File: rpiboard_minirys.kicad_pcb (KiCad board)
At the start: 4 copper layers, 65 x 56.5 mm, 92 parts, among them IC1 LM51231QRGRRQ1, IC2 TPS564242DRLR, IC3 L6470HTR, IC4 L6470HTR, J1 RPi_GPIO, J10 ToF1_Sensor, J11 ToF2_Sensor, J12 ToF3_Sensor, J13 ToF4_Sensor, J14 ToF5_Sensor, J15 ToF6_Sensor, J16 SPI_Interface, J17 UART_Interface, J18 Fan_Interface, J2 Motor_L, J3 Motor_R, J4 B_Cell_3, J5 B_Cell_2, J6 B_Cell_1, J7 SW, J8 Temp_Sensor, J9 IMU_Sensor, Q1 ISK057N04LM6ATLA1, Q2 ISK057N04LM6ATLA1

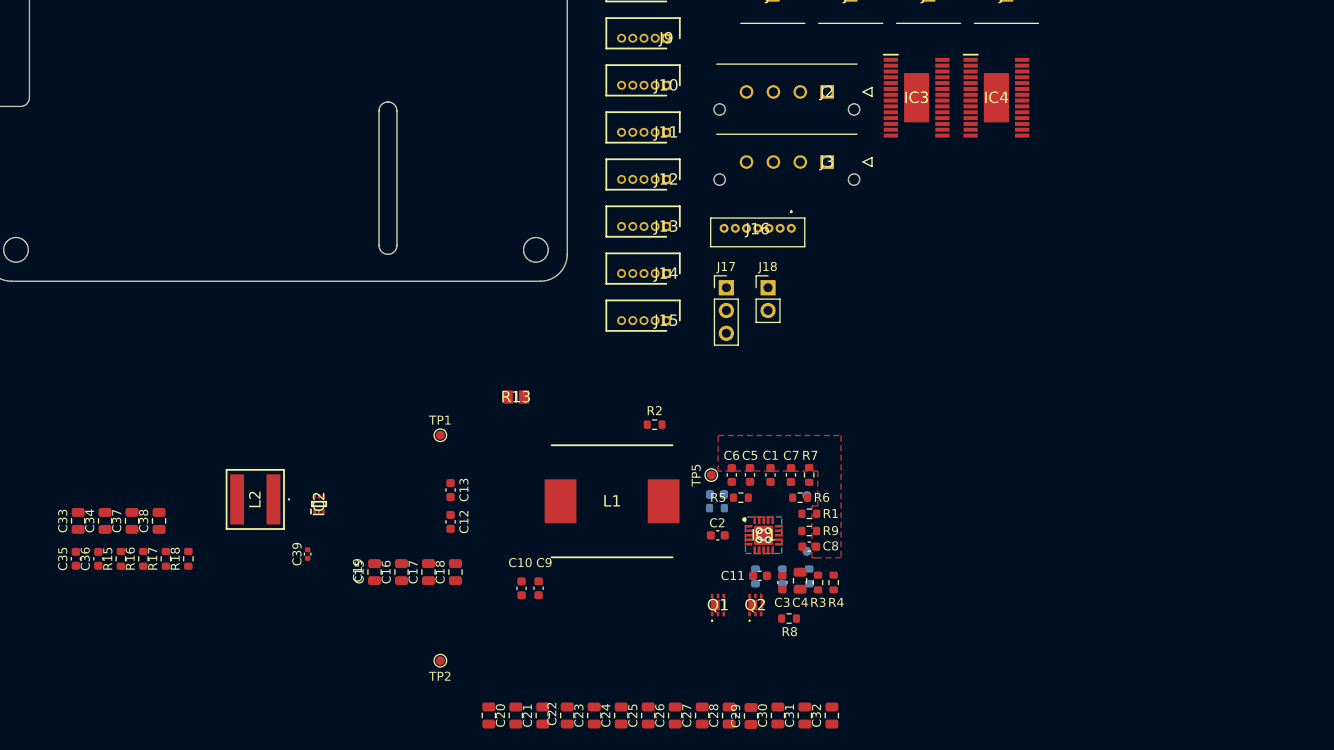
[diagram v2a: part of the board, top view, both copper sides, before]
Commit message: New complete schematic version
May need to resize the resistors, also need to change the caps back to electrolytic
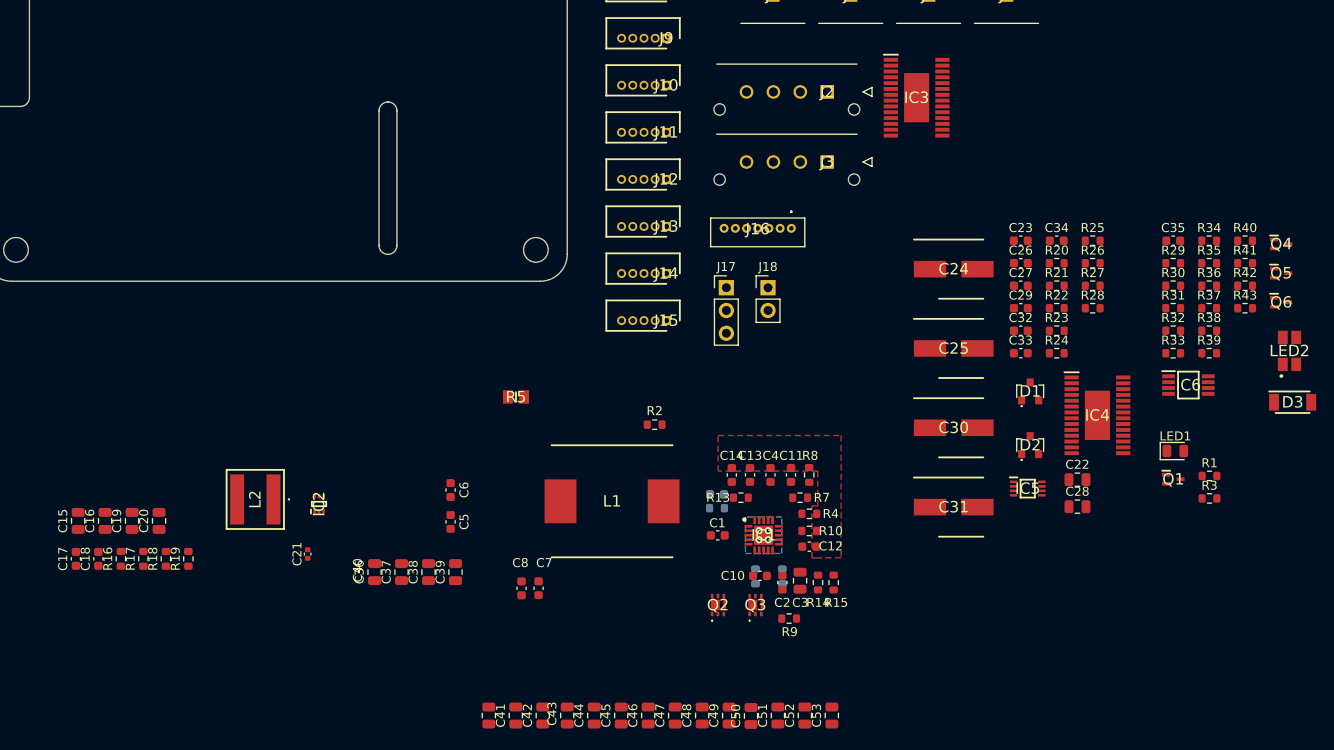
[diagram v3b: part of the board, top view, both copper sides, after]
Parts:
- removed the R12 at (197.5, 143.7)
- removed TP1: TestPoint_VCC, TestPoint:TestPoint_Pad_D1.0mm
- removed TP2: TestPoint_VOUT, TestPoint:TestPoint_Pad_D1.0mm
- removed TP3: TestPoint_TRK, TestPoint:TestPoint_Pad_D1.0mm
- removed TP4: TestPoint_UVLO, TestPoint:TestPoint_Pad_D1.0mm
- removed TP5: TestPoint_SW, TestPoint:TestPoint_Pad_D1.0mm
- added C22: 10uF, Capacitor_SMD:C_0805_2012Metric, F.Cu at (227.4, 132.9)
- added C23: 10nF, Capacitor_SMD:C_0603_1608Metric, F.Cu at (221.1, 106.2)
- added C24: 47uF, parts:CAPAE660X850N, F.Cu at (213.6, 109.4)
- added C25: 47uF, parts:CAPAE660X850N, F.Cu at (213.6, 118.2)
- added C26: 100nF, Capacitor_SMD:C_0603_1608Metric, F.Cu at (221.1, 108.7)
- added C27: 100nF, Capacitor_SMD:C_0603_1608Metric, F.Cu at (221.1, 111.2)
- added C28: 10uF, Capacitor_SMD:C_0805_2012Metric, F.Cu at (227.4, 135.9)
- added C29: 10nF, Capacitor_SMD:C_0603_1608Metric, F.Cu at (221.1, 113.8)
- added C30: 47uF, parts:CAPAE660X850N, F.Cu at (213.6, 127.1)
- added C31: 47uF, parts:CAPAE660X850N, F.Cu at (213.6, 135.9)
- added C32: 100nF, Capacitor_SMD:C_0603_1608Metric, F.Cu at (221.1, 116.3)
- added C33: 100nF, Capacitor_SMD:C_0603_1608Metric, F.Cu at (221.1, 118.8)
- added C34: 100nF, Capacitor_SMD:C_0603_1608Metric, F.Cu at (225.1, 106.2)
- added C35: 100nF, Capacitor_SMD:C_0603_1608Metric, F.Cu at (238.1, 106.2)
- added D1: BAV99, parts:ZXMP6A13FTA, F.Cu at (222.1, 123.0)
- added D2: BAV99, parts:ZXMP6A13FTA, F.Cu at (222.1, 129.0)
- added D3: STPST1H100AF, parts:SODFL4724X103N, F.Cu at (251.4, 124.2)
- added IC5: 74AUP2G00DC,125, parts:SOP50P310X100-8N, F.Cu at (221.9, 133.9)
- added IC6: MAX11613EUA+T, parts:SOP65P490X110-8N, F.Cu at (239.8, 122.3)
- added LED1: GREEN, Diode_SMD:D_0805_2012Metric, F.Cu at (238.3, 129.7)
- added LED2: LSG_T676-P7Q7-1+N7P7-24, parts:LSGT676P7Q71N7P724, F.Cu at (251.1, 118.5)
- added Q1: DMG1012T-7, parts:SOT50P160X80-3N, F.Cu at (238.1, 132.8)
- added Q4: DMG1012T-7, parts:SOT50P160X80-3N, F.Cu at (250.2, 106.6)
- added Q5: DMG1012T-7, parts:SOT50P160X80-3N, F.Cu at (250.2, 109.8)
- added Q6: DMG1012T-7, parts:SOT50P160X80-3N, F.Cu at (250.2, 113.1)
- added R1: 100R, Resistor_SMD:R_0603_1608Metric, F.Cu at (242.2, 132.5)
- added R20: 10k, Resistor_SMD:R_0603_1608Metric, F.Cu at (225.1, 108.7)
- added R21: 27k, Resistor_SMD:R_0603_1608Metric, F.Cu at (225.1, 111.2)
- added R22: 10k, Resistor_SMD:R_0603_1608Metric, F.Cu at (225.1, 113.8)
- added R23: 27k, Resistor_SMD:R_0603_1608Metric, F.Cu at (225.1, 116.3)
- added R24: 38.3k, Resistor_SMD:R_0603_1608Metric, F.Cu at (225.1, 118.8)
- added R25: 38.3k, Resistor_SMD:R_0603_1608Metric, F.Cu at (229.1, 106.2)
- added R26: 38.3k, Resistor_SMD:R_0603_1608Metric, F.Cu at (229.1, 108.7)
- added R27: 38.3k, Resistor_SMD:R_0603_1608Metric, F.Cu at (229.1, 111.2)
- added R28: 38.3k, Resistor_SMD:R_0603_1608Metric, F.Cu at (229.1, 113.8)
- added R29: 100k, Resistor_SMD:R_0603_1608Metric, F.Cu at (238.1, 108.7)
- added R3: 150R, Resistor_SMD:R_0603_1608Metric, F.Cu at (242.2, 135.0)
- added R30: 150R, Resistor_SMD:R_0603_1608Metric, F.Cu at (238.1, 111.2)
- added R31: 15k, Resistor_SMD:R_0603_1608Metric, F.Cu at (238.1, 113.8)
- added R32: 10k, Resistor_SMD:R_0603_1608Metric, F.Cu at (238.1, 116.3)
- added R33: 36k, Resistor_SMD:R_0603_1608Metric, F.Cu at (238.1, 118.8)
- added R34: 10k, Resistor_SMD:R_0603_1608Metric, F.Cu at (242.1, 106.2)
- added R35: 56k, Resistor_SMD:R_0603_1608Metric, F.Cu at (242.1, 108.7)
- added R36: 10k, Resistor_SMD:R_0603_1608Metric, F.Cu at (242.1, 111.2)
- added R37: 10k, Resistor_SMD:R_0603_1608Metric, F.Cu at (242.1, 113.8)
- added R38: 100k, Resistor_SMD:R_0603_1608Metric, F.Cu at (242.1, 116.3)
- added R39: 150R, Resistor_SMD:R_0603_1608Metric, F.Cu at (242.1, 118.8)
- added R40: 150R, Resistor_SMD:R_0603_1608Metric, F.Cu at (246.1, 106.2)
- added R41: 150R, Resistor_SMD:R_0603_1608Metric, F.Cu at (246.1, 108.7)
- added R42: 150R, Resistor_SMD:R_0603_1608Metric, F.Cu at (246.1, 111.2)
- added R43: 100k, Resistor_SMD:R_0603_1608Metric, F.Cu at (246.1, 113.8)
- J16: value SPI_Interface -> SPI_Connector
- J17: value UART_Interface -> UART_Connector
- J18: value Fan_Interface -> Fan_Connector
- R2: value 100k -> 12k
- moved IC4 37.2 mm to (229.6, 125.7)
- renumbered C2 to C1, C11 to C10, C7 to C11, C8 to C12, C5 to C13, C6 to C14, C33 to C15, C34 to C16, C35 to C17, C36 to C18, C37 to C19, C3 to C2, C38 to C20, C39 to C21, C4 to C3, C15 to C36, C16 to C37, C17 to C38, C18 to C39, C1 to C4, C19 to C40, C20 to C41, C21 to C42, C22 to C43, C23 to C44, C24 to C45, C25 to C46, C26 to C47, C27 to C48, C28 to C49, C12 to C5, C29 to C50, C30 to C51, C31 to C52, C32 to C53, C13 to C6, C9 to C7, C10 to C8, C14 to C9, Q1 to Q2, Q2 to Q3, R9 to R10, R10 to R11, R11 to R12, R5 to R13, R3 to R14, R4 to R15, R15 to R16, R16 to R17, R17 to R18, R18 to R19, R1 to R4, R13 to R5, R14 to R6, R6 to R7, R7 to R8, R8 to R9
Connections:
- net /Supply_24V/PGOOD renamed Net-(IC1-PGOOD)
- C1 pad 2: /Supply_24V/VOUT -> +24V
- C18 pad 1: /Supply_5V/+5V -> +5V
- C19 pad 1: /Supply_5V/+5V -> +5V
- C20 pad 1: /Supply_5V/+5V -> +5V
- C21 pad 2: /Supply_5V/+5V -> +5V
- C41 pad 1: /Supply_24V/VOUT -> +24V
- C42 pad 1: /Supply_24V/VOUT -> +24V
- C43 pad 1: /Supply_24V/VOUT -> +24V
- C44 pad 1: /Supply_24V/VOUT -> +24V
- C45 pad 1: /Supply_24V/VOUT -> +24V
- C46 pad 1: /Supply_24V/VOUT -> +24V
- C47 pad 1: /Supply_24V/VOUT -> +24V
- C48 pad 1: /Supply_24V/VOUT -> +24V
- C49 pad 1: /Supply_24V/VOUT -> +24V
- C50 pad 1: /Supply_24V/VOUT -> +24V
- C51 pad 1: /Supply_24V/VOUT -> +24V
- C52 pad 1: /Supply_24V/VOUT -> +24V
- C53 pad 1: /Supply_24V/VOUT -> +24V
- C7 pad 1: /Supply_24V/VOUT -> +24V
- C8 pad 1: /Supply_24V/VOUT -> +24V
- IC1 pad 3: /Supply_24V/VOUT -> +24V
- IC3 pad 1: unconnected-(IC3-OUT1A-Pad1) -> /Connectors/ML_OUT1A
- IC3 pad 10: unconnected-(IC3-CP-Pad10) -> /Motor_Controllers/ML_CP
- IC3 pad 11: unconnected-(IC3-VBOOT-Pad11) -> /Motor_Controllers/ML_VBOOT
- IC3 pad 12: unconnected-(IC3-VSB_1-Pad12) -> +24V
- IC3 pad 13: unconnected-(IC3-PGND_1-Pad13) -> GND
- IC3 pad 14: unconnected-(IC3-OUT1B-Pad14) -> /Connectors/ML_OUT1B
- IC3 pad 15: unconnected-(IC3-OUT2B-Pad15) -> /Connectors/ML_OUT2B
- IC3 pad 16: unconnected-(IC3-VSB_2-Pad16) -> +24V
- IC3 pad 17: unconnected-(IC3-VDD-Pad17) -> +3.3V
- IC3 pad 18: unconnected-(IC3-SDO-Pad18) -> /Motor_Controllers/SPI_BRIDGE
- IC3 pad 19: unconnected-(IC3-CK-Pad19) -> /Connectors/SPI_CLK
- IC3 pad 2: unconnected-(IC3-VSA_1-Pad2) -> +24V
- IC3 pad 20: unconnected-(IC3-SDI-Pad20) -> /Connectors/SPI_MOSI
- IC3 pad 21: unconnected-(IC3-DGND-Pad21) -> GND
- IC3 pad 22: unconnected-(IC3-~{BUSY}/SYNC-Pad22) -> /Motor_Controllers/~{ML_BUSY}
- IC3 pad 23: unconnected-(IC3-~{CS}-Pad23) -> /Connectors/~{SPI_CS_M}
- IC3 pad 24: unconnected-(IC3-~{FLAG}-Pad24) -> /Motor_Controllers/~{ML_FLAG}
- IC3 pad 26: unconnected-(IC3-VSA_2-Pad26) -> +24V
- IC3 pad 27: unconnected-(IC3-PGND_2-Pad27) -> GND
- IC3 pad 28: unconnected-(IC3-OUT2A-Pad28) -> /Connectors/ML_OUT2A
- IC3 pad 29: unconnected-(IC3-EP-Pad29) -> GND
- IC3 pad 3: unconnected-(IC3-~{STBY}/RST-Pad3) -> /Connectors/~{M_STBY}
- IC3 pad 4: unconnected-(IC3-SW-Pad4) -> +3.3V
- IC3 pad 5: unconnected-(IC3-ADCIN-Pad5) -> /Motor_Controllers/ML_ADCIN
- IC3 pad 6: unconnected-(IC3-VREG-Pad6) -> +3.3V
- IC3 pad 8: unconnected-(IC3-OSCOUT-Pad8) -> /Motor_Controllers/OSCOUT
- IC3 pad 9: unconnected-(IC3-AGND-Pad9) -> GND
- IC4 pad 1: unconnected-(IC4-OUT1A-Pad1) -> /Connectors/MR_OUT1A
- IC4 pad 10: unconnected-(IC4-CP-Pad10) -> /Motor_Controllers/MR_CP
- IC4 pad 11: unconnected-(IC4-VBOOT-Pad11) -> /Motor_Controllers/MR_VBOOT
- IC4 pad 12: unconnected-(IC4-VSB_1-Pad12) -> +24V
- IC4 pad 13: unconnected-(IC4-PGND_1-Pad13) -> GND
- IC4 pad 14: unconnected-(IC4-OUT1B-Pad14) -> /Connectors/MR_OUT1B
- IC4 pad 15: unconnected-(IC4-OUT2B-Pad15) -> /Connectors/MR_OUT2B
- IC4 pad 16: unconnected-(IC4-VSB_2-Pad16) -> +24V
- IC4 pad 17: unconnected-(IC4-VDD-Pad17) -> +3.3V
- IC4 pad 18: unconnected-(IC4-SDO-Pad18) -> /Connectors/SPI_MISO
- IC4 pad 19: unconnected-(IC4-CK-Pad19) -> /Connectors/SPI_CLK
- IC4 pad 2: unconnected-(IC4-VSA_1-Pad2) -> +24V
- IC4 pad 20: unconnected-(IC4-SDI-Pad20) -> /Motor_Controllers/SPI_BRIDGE
- IC4 pad 21: unconnected-(IC4-DGND-Pad21) -> GND
- IC4 pad 22: unconnected-(IC4-~{BUSY}/SYNC-Pad22) -> /Motor_Controllers/~{MR_BUSY}
- IC4 pad 23: unconnected-(IC4-~{CS}-Pad23) -> /Connectors/~{SPI_CS_M}
- IC4 pad 24: unconnected-(IC4-~{FLAG}-Pad24) -> /Motor_Controllers/~{MR_FLAG}
- IC4 pad 26: unconnected-(IC4-VSA_2-Pad26) -> +24V
- IC4 pad 27: unconnected-(IC4-PGND_2-Pad27) -> GND
- IC4 pad 28: unconnected-(IC4-OUT2A-Pad28) -> /Connectors/MR_OUT2A
- IC4 pad 29: unconnected-(IC4-EP-Pad29) -> GND
- IC4 pad 3: unconnected-(IC4-~{STBY}/RST-Pad3) -> /Connectors/~{M_STBY}
- IC4 pad 4: unconnected-(IC4-SW-Pad4) -> +3.3V
- IC4 pad 5: unconnected-(IC4-ADCIN-Pad5) -> /Motor_Controllers/MR_ADCIN
- IC4 pad 6: unconnected-(IC4-VREG-Pad6) -> +3.3V
- IC4 pad 8: unconnected-(IC4-OSCOUT-Pad8) -> /Motor_Controllers/OSCOUT
- IC4 pad 9: unconnected-(IC4-AGND-Pad9) -> GND
- J1 pad 1: unconnected-(J1-Pin_1-Pad1) -> +3.3V
- J1 pad 10: unconnected-(J1-Pin_10-Pad10) -> /Connectors/UART_RX
- J1 pad 11: unconnected-(J1-Pin_11-Pad11) -> /Connectors/M_FLAG
- J1 pad 12: unconnected-(J1-Pin_12-Pad12) -> /Connectors/FAN_PWM
- J1 pad 13: unconnected-(J1-Pin_13-Pad13) -> /Connectors/M_BUSY
- J1 pad 14: unconnected-(J1-Pin_14-Pad14) -> GND
- J1 pad 15: unconnected-(J1-Pin_15-Pad15) -> /Connectors/~{M_STBY}
- J1 pad 16: unconnected-(J1-Pin_16-Pad16) -> /Connectors/LED_RED
- J1 pad 17: unconnected-(J1-Pin_17-Pad17) -> +3.3V
- J1 pad 18: unconnected-(J1-Pin_18-Pad18) -> /Connectors/LED_GREEN
- J1 pad 19: unconnected-(J1-Pin_19-Pad19) -> /Connectors/SPI_MOSI
- J1 pad 2: unconnected-(J1-Pin_2-Pad2) -> +5V
- J1 pad 20: unconnected-(J1-Pin_20-Pad20) -> GND
- J1 pad 21: unconnected-(J1-Pin_21-Pad21) -> /Connectors/SPI_MISO
- J1 pad 22: unconnected-(J1-Pin_22-Pad22) -> /Connectors/SPI_IRQ
- J1 pad 23: unconnected-(J1-Pin_23-Pad23) -> /Connectors/SPI_CLK
- J1 pad 24: unconnected-(J1-Pin_24-Pad24) -> /Connectors/~{SPI_CS_M}
- J1 pad 25: unconnected-(J1-Pin_25-Pad25) -> GND
- J1 pad 26: unconnected-(J1-Pin_26-Pad26) -> /Connectors/~{SPI_CS_E}
- J1 pad 29: unconnected-(J1-Pin_29-Pad29) -> /Connectors/I2C3_SCL
- J1 pad 3: unconnected-(J1-Pin_3-Pad3) -> /Connectors/I2C1_SDA
- J1 pad 30: unconnected-(J1-Pin_30-Pad30) -> GND
- J1 pad 31: unconnected-(J1-Pin_31-Pad31) -> /Connectors/TOF1_EN
- J1 pad 32: unconnected-(J1-Pin_32-Pad32) -> /Connectors/I2C5_SDA
- J1 pad 33: unconnected-(J1-Pin_33-Pad33) -> /Connectors/I2C5_SCL
- J1 pad 34: unconnected-(J1-Pin_34-Pad34) -> GND
- J1 pad 35: unconnected-(J1-Pin_35-Pad35) -> /Connectors/TOF3_EN
- J1 pad 36: unconnected-(J1-Pin_36-Pad36) -> /Connectors/TOF2_EN
- J1 pad 37: unconnected-(J1-Pin_37-Pad37) -> /Connectors/TOF6_EN
- J1 pad 38: unconnected-(J1-Pin_38-Pad38) -> /Connectors/TOF4_EN
- J1 pad 39: unconnected-(J1-Pin_39-Pad39) -> GND
- J1 pad 4: unconnected-(J1-Pin_4-Pad4) -> +5V
- J1 pad 40: unconnected-(J1-Pin_40-Pad40) -> /Connectors/TOF5_EN
- J1 pad 5: unconnected-(J1-Pin_5-Pad5) -> /Connectors/I2C1_SCL
- J1 pad 6: unconnected-(J1-Pin_6-Pad6) -> GND
- J1 pad 7: unconnected-(J1-Pin_7-Pad7) -> /Connectors/I2C3_SDA
- J1 pad 8: unconnected-(J1-Pin_8-Pad8) -> /Connectors/UART_TX
- J1 pad 9: unconnected-(J1-Pin_9-Pad9) -> GND
- J10 pad 1: unconnected-(J10-Pin_1-Pad1) -> GND
- J10 pad 2: unconnected-(J10-Pin_2-Pad2) -> /Connectors/TOF1_EN
- J10 pad 3: unconnected-(J10-Pin_3-Pad3) -> /Connectors/I2C3_SCL
- J10 pad 4: unconnected-(J10-Pin_4-Pad4) -> /Connectors/I2C3_SDA
- J10 pad 5: unconnected-(J10-Pin_5-Pad5) -> +5V
- J11 pad 1: unconnected-(J11-Pin_1-Pad1) -> GND
- J11 pad 2: unconnected-(J11-Pin_2-Pad2) -> /Connectors/TOF2_EN
- J11 pad 3: unconnected-(J11-Pin_3-Pad3) -> /Connectors/I2C3_SCL
- J11 pad 4: unconnected-(J11-Pin_4-Pad4) -> /Connectors/I2C3_SDA
- J11 pad 5: unconnected-(J11-Pin_5-Pad5) -> +5V
- J12 pad 1: unconnected-(J12-Pin_1-Pad1) -> GND
- J12 pad 2: unconnected-(J12-Pin_2-Pad2) -> /Connectors/TOF3_EN
- J12 pad 3: unconnected-(J12-Pin_3-Pad3) -> /Connectors/I2C3_SCL
- J12 pad 4: unconnected-(J12-Pin_4-Pad4) -> /Connectors/I2C3_SDA
- J12 pad 5: unconnected-(J12-Pin_5-Pad5) -> +5V
- J13 pad 1: unconnected-(J13-Pin_1-Pad1) -> GND
- J13 pad 2: unconnected-(J13-Pin_2-Pad2) -> /Connectors/TOF4_EN
- J13 pad 3: unconnected-(J13-Pin_3-Pad3) -> /Connectors/I2C5_SCL
- J13 pad 4: unconnected-(J13-Pin_4-Pad4) -> /Connectors/I2C5_SDA
- J13 pad 5: unconnected-(J13-Pin_5-Pad5) -> +5V
- J14 pad 1: unconnected-(J14-Pin_1-Pad1) -> GND
- J14 pad 2: unconnected-(J14-Pin_2-Pad2) -> /Connectors/TOF5_EN
- J14 pad 3: unconnected-(J14-Pin_3-Pad3) -> /Connectors/I2C5_SCL
- J14 pad 4: unconnected-(J14-Pin_4-Pad4) -> /Connectors/I2C5_SDA
- J14 pad 5: unconnected-(J14-Pin_5-Pad5) -> +5V
- J15 pad 1: unconnected-(J15-Pin_1-Pad1) -> GND
- J15 pad 2: unconnected-(J15-Pin_2-Pad2) -> /Connectors/TOF6_EN
- J15 pad 3: unconnected-(J15-Pin_3-Pad3) -> /Connectors/I2C5_SCL
- J15 pad 4: unconnected-(J15-Pin_4-Pad4) -> /Connectors/I2C5_SDA
- J15 pad 5: unconnected-(J15-Pin_5-Pad5) -> +5V
- J16 pad 1: unconnected-(J16-Pin_1-Pad1) -> GND
- J16 pad 2: unconnected-(J16-Pin_2-Pad2) -> /Connectors/SPI_IRQ
- J16 pad 3: unconnected-(J16-Pin_3-Pad3) -> /Connectors/~{SPI_CS_E}
- J16 pad 4: unconnected-(J16-Pin_4-Pad4) -> /Connectors/SPI_CLK
- J16 pad 5: unconnected-(J16-Pin_5-Pad5) -> /Connectors/SPI_MISO
- J16 pad 6: unconnected-(J16-Pin_6-Pad6) -> /Connectors/SPI_MOSI
- J16 pad 7: unconnected-(J16-Pin_7-Pad7) -> +5V
- J17 pad 1: unconnected-(J17-Pin_1-Pad1) -> GND
- J17 pad 2: unconnected-(J17-Pin_2-Pad2) -> /Connectors/UART_TX
- J17 pad 3: unconnected-(J17-Pin_3-Pad3) -> /Connectors/UART_RX
- J18 pad 1: unconnected-(J18-Pin_1-Pad1) -> /Connectors/FAN_SW
- J18 pad 2: unconnected-(J18-Pin_2-Pad2) -> +5V
- J2 pad 1: unconnected-(J2-Pin_1-Pad1) -> /Connectors/ML_OUT2A
- J2 pad 2: unconnected-(J2-Pin_2-Pad2) -> /Connectors/ML_OUT1A
- J2 pad 3: unconnected-(J2-Pin_3-Pad3) -> /Connectors/ML_OUT1B
- J2 pad 4: unconnected-(J2-Pin_4-Pad4) -> /Connectors/ML_OUT2B
- J3 pad 1: unconnected-(J3-Pin_1-Pad1) -> /Connectors/MR_OUT2A
- J3 pad 2: unconnected-(J3-Pin_2-Pad2) -> /Connectors/MR_OUT1A
- J3 pad 3: unconnected-(J3-Pin_3-Pad3) -> /Connectors/MR_OUT1B
- J3 pad 4: unconnected-(J3-Pin_4-Pad4) -> /Connectors/MR_OUT2B
- J4 pad 1: unconnected-(J4-Pin_1-Pad1) -> /Connectors/CELL_2
- J4 pad 2: unconnected-(J4-Pin_2-Pad2) -> /Connectors/CELL_3
- J5 pad 1: unconnected-(J5-Pin_1-Pad1) -> /Connectors/CELL_1
- J5 pad 2: unconnected-(J5-Pin_2-Pad2) -> /Connectors/CELL_2
- J6 pad 1: unconnected-(J6-Pin_1-Pad1) -> Net-(J6-Pin_1)
- J6 pad 2: unconnected-(J6-Pin_2-Pad2) -> /Connectors/CELL_1
- J7 pad 1: unconnected-(J7-Pin_1-Pad1) -> GND
- J7 pad 2: unconnected-(J7-Pin_2-Pad2) -> Net-(J6-Pin_1)
- J8 pad 1: unconnected-(J8-Pin_1-Pad1) -> GND
- J8 pad 3: unconnected-(J8-Pin_3-Pad3) -> /Connectors/I2C1_SCL
- J8 pad 4: unconnected-(J8-Pin_4-Pad4) -> /Connectors/I2C1_SDA
- J8 pad 5: unconnected-(J8-Pin_5-Pad5) -> +5V
- J9 pad 1: unconnected-(J9-Pin_1-Pad1) -> GND
- J9 pad 3: unconnected-(J9-Pin_3-Pad3) -> /Connectors/I2C1_SCL
- J9 pad 4: unconnected-(J9-Pin_4-Pad4) -> /Connectors/I2C1_SDA
- J9 pad 5: unconnected-(J9-Pin_5-Pad5) -> +5V
- L2 pad 1: /Supply_5V/+5V -> +5V
- Q2 pad 1: /Supply_24V/VOUT -> +24V
- Q2 pad 2: /Supply_24V/VOUT -> +24V
- Q2 pad 5: /Supply_24V/VOUT -> +24V
- Q2 pad 6: /Supply_24V/VOUT -> +24V
- Q2 pad 8: /Supply_24V/VOUT -> +24V
- R18 pad 1: /Supply_5V/+5V -> +5V
- R2 pad 2: /Supply_24V/VCC_MCU -> +5V

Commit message: Uploaded all project files, finished PCB design
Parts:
- removed C45, C46, C47, C48, C49, C50, C51, C52, C53: 22uF, Capacitor_SMD:C_0805_2012Metric
- removed R43: 100k, Resistor_SMD:R_0603_1608Metric
- added F1: 10A Fuse, parts:FUSC6126X270N, B.Cu at (63.0, 34.2)
- C11: footprint Capacitor_SMD:C_0603_1608Metric -> Capacitor_SMD:C_0402_1005Metric
- C13: value 100pF -> 22pF; footprint Capacitor_SMD:C_0603_1608Metric -> Capacitor_SMD:C_0402_1005Metric
- C14: value 6.8nF -> 1.5nF; footprint Capacitor_SMD:C_0603_1608Metric -> Capacitor_SMD:C_0402_1005Metric
- C15: value 10uF -> 100uF; footprint Capacitor_SMD:C_0805_2012Metric -> parts:CAPAE1030X1100N
- C17: value 100nF -> 10uF; footprint Capacitor_SMD:C_0603_1608Metric -> Capacitor_SMD:C_0805_2012Metric
- C18, C33: value 100nF -> 100uF; footprint Capacitor_SMD:C_0603_1608Metric -> parts:CAPAE1030X1100N
- C19, C20: value 22uF -> 10uF/50V; footprint Capacitor_SMD:C_0805_2012Metric -> Capacitor_SMD:C_1206_3216Metric
- C21: value 33pF -> 100nF; footprint Capacitor_SMD:C_0402_1005Metric -> Capacitor_SMD:C_0603_1608Metric; moved to B.Cu
- C22, C35, IC2, IC5, IC6, L2, Q1, Q4, Q5, R14, R2, R24, R25, R26, R27, R37: moved to B.Cu
- C23: value 10nF -> 10uF; footprint Capacitor_SMD:C_0603_1608Metric -> Capacitor_SMD:C_0805_2012Metric; moved to B.Cu
- C24, C25: value 47uF -> 10uF; footprint parts:CAPAE660X850N -> Capacitor_SMD:C_0805_2012Metric; moved to B.Cu
- C26, C27: value 100nF -> 10uF; footprint Capacitor_SMD:C_0603_1608Metric -> Capacitor_SMD:C_0805_2012Metric; moved to B.Cu
- C28: value 10uF -> 100nF; footprint Capacitor_SMD:C_0805_2012Metric -> Capacitor_SMD:C_0603_1608Metric; moved to B.Cu
- C29: value 10nF -> 33pF; footprint Capacitor_SMD:C_0603_1608Metric -> Capacitor_SMD:C_0402_1005Metric; moved to B.Cu
- C30: value 47uF -> 10uF; footprint parts:CAPAE660X850N -> Capacitor_SMD:C_0805_2012Metric
- C31: value 47uF -> 220nF; footprint parts:CAPAE660X850N -> Capacitor_SMD:C_0805_2012Metric; moved to B.Cu
- C32: value 100nF -> 10nF; moved to B.Cu
- C34: value 100nF -> 220nF; footprint Capacitor_SMD:C_0603_1608Metric -> Capacitor_SMD:C_0805_2012Metric; moved to B.Cu
- C36: value 22uF -> 10uF
- C37, C40: value 22uF -> 220nF; moved to B.Cu
- C38: value 22uF -> 10nF; footprint Capacitor_SMD:C_0805_2012Metric -> Capacitor_SMD:C_0603_1608Metric; moved to B.Cu
- C39: value 22uF -> 100uF; footprint Capacitor_SMD:C_0805_2012Metric -> parts:CAPAE1030X1100N
- C41, C42, C44: value 22uF -> 100nF; footprint Capacitor_SMD:C_0805_2012Metric -> Capacitor_SMD:C_0603_1608Metric; moved to B.Cu
- C43: value 22uF -> 4.7uF; moved to B.Cu
- C9: footprint Capacitor_SMD:C_0603_1608Metric -> Capacitor_SMD:C_0402_1005Metric; moved to F.Cu
- D1, D2: footprint parts:ZXMP6A13FTA -> parts:BAV99215; moved to B.Cu
- D3: value STPST1H100AF -> BAT54GWX; footprint parts:SODFL4724X103N -> parts:SOD123
- IC3, IC4: value L6470HTR -> L6470H
- J17: footprint Connector_PinHeader_2.54mm:PinHeader_1x03_P2.54mm_Vertical -> parts:SHDR5W27P0X125_1X5_800X320X440P
- J18: footprint Connector_PinHeader_2.54mm:PinHeader_1x02_P2.54mm_Vertical -> Connector_PinHeader_2.54mm:PinHeader_1x02_P2.54mm_Vertical_SMD_Pin1Left
- L1: value SRP1265CC-150M -> SRP6060FA-4R7M; footprint parts:INDPM135125X650N -> parts:SRP6060FA4R7M
- LED1: footprint Diode_SMD:D_0805_2012Metric -> LED_SMD:LED_0805_2012Metric
- Q2, Q3: value ISK057N04LM6ATLA1 -> ISZ065N03L5S; footprint parts:ISK057N04LM6ATLA1 -> parts:ISZ065N03L5SATMA1
- R1: value 100R -> 150R
- R10: value 12k -> 0R; moved to B.Cu
- R12: value 0R -> 59k; moved to F.Cu
- R13: value 38.3k -> 0R; moved to B.Cu
- R15: value 0R -> 220k; moved to B.Cu
- R16: value 100k -> 30k; moved to B.Cu
- R17: value 17.4k -> 100k; moved to B.Cu
- R18: value 220k -> 17.4k; moved to B.Cu
- R19: value 30k -> 27k
- R23: value 27k -> 38.3k; moved to B.Cu
- R28: value 38.3k -> 100k; moved to B.Cu
- R29: value 100k -> 150R; moved to B.Cu
- R3: value 150R -> 32.4k/.1%
- R31: value 15k -> 150R
- R32: value 10k -> 150R; moved to B.Cu
- R33: value 36k -> 100k; moved to B.Cu
- R34: value 10k -> 100k
- R35: value 56k -> 150R
- R36: value 10k -> 15k; moved to B.Cu
- R38: value 100k -> 36k; moved to B.Cu
- R39, R41, R42: value 150R -> 10k; moved to B.Cu
- R4: value 80.6k -> 0.006R; footprint Resistor_SMD:R_0603_1608Metric -> Resistor_SMD:R_0805_2012Metric
- R40: value 150R -> 56k; moved to B.Cu
- R5: value WFC08056L000FE66 -> 100R; footprint parts:RESC2013X85N -> Resistor_SMD:R_0603_1608Metric
- R6: value 100R -> 21k; moved to F.Cu
- R7: value 21k -> 14k
- R8: value 14k -> 80.6k
- R9: value 80.6k -> 12k
- moved R42 222.4 mm to (28.9, 63.7), turned to 90 degrees
- moved IC6 216.8 mm to (31.6, 62.0), turned to 90 degrees
- moved R37 214.2 mm to (34.6, 60.5), turned to 90 degrees
- moved R39 213.9 mm to (36.4, 60.5), turned to 90 degrees
- moved R41 213.6 mm to (38.1, 60.5), turned to 90 degrees
- moved R36 212.9 mm to (34.6, 63.7), turned to 90 degrees
- moved R38 212.4 mm to (36.4, 63.7), turned to 90 degrees
- moved R40 212.3 mm to (38.1, 63.7), turned to 90 degrees
- moved C31 206.7 mm to (31.0, 39.2), turned to -90 degrees
- moved C35 206.6 mm to (39.3, 49.9), turned to 90 degrees
- moved D1 206.2 mm to (33.8, 39.2), turned to 90 degrees
- moved R20 205.5 mm to (29.6, 45.6), turned to 90 degrees
- moved IC5 202.9 mm to (42.0, 39.9), turned to 90 degrees
- moved C32 200.2 mm to (36.3, 39.3), turned to -90 degrees
- moved C30 200.1 mm to (29.4, 49.0), turned to -90 degrees
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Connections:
- C18 pad 1: +5V -> +24V
- C19 pad 1: +5V -> +24V
- C20 pad 1: +5V -> +24V
- C21 pad 1: Net-(IC2-FB) -> +5V
- C21 pad 2: +5V -> GND
- C22 pad 1: +3.3V -> +5V
- C23 pad 1: Net-(D1-common) -> +5V
- C23 pad 2: /Motor_Controllers/ML_CP -> GND
- C24 pad 1: +24V -> +5V
- C24 pad 2: Net-(C24-Pad2) -> GND
- C25 pad 1: +24V -> +5V
- C25 pad 2: Net-(C24-Pad2) -> GND
- C26 pad 1: Net-(C24-Pad2) -> VCC
- C26 pad 2: +24V -> GND
- C27 pad 1: GND -> VCC
- C27 pad 2: +3.3V -> GND
- C28 pad 1: +3.3V -> VCC
- C29 pad 1: Net-(D2-common) -> Net-(IC2-FB)
- C29 pad 2: /Motor_Controllers/MR_CP -> +5V
- C3 pad 1: /Supply_24V/VCC_DRIVER -> /Supply_24V/VCC_REG
- C30 pad 1: +24V -> +3.3V
- C30 pad 2: Net-(C30-Pad2) -> GND
- C31 pad 1: +24V -> /Motor_Controllers/ML_VBOOT
- C31 pad 2: Net-(C30-Pad2) -> +24V
- C32 pad 1: Net-(C30-Pad2) -> Net-(D1-common)
- C32 pad 2: +24V -> /Motor_Controllers/ML_CP
- C33 pad 1: GND -> +24V
- C33 pad 2: +3.3V -> GND
- C34 pad 1: +3.3V -> GND
- C34 pad 2: GND -> +24V
- C35 pad 1: +3.3V -> GND
- C35 pad 2: GND -> +3.3V
- C36 pad 1: VCC -> +3.3V
- C37 pad 1: VCC -> /Motor_Controllers/MR_VBOOT
- C37 pad 2: GND -> +24V
- C38 pad 1: VCC -> Net-(D2-common)
- C38 pad 2: GND -> /Motor_Controllers/MR_CP
- C39 pad 1: VCC -> +24V
- C40 pad 1: VCC -> GND
- C40 pad 2: GND -> +24V
- C41 pad 1: +24V -> GND
- C41 pad 2: GND -> +3.3V
- C42 pad 1: +24V -> +3.3V
- C43 pad 1: +24V -> +3.3V
- C44 pad 1: +24V -> +3.3V
- IC1 pad 9: /Supply_24V/VCC_DRIVER -> /Supply_24V/VCC_REG
- IC3 pad 8: /Motor_Controllers/OSCOUT -> /Motor_Controllers/CLK_SYNC
- IC4 pad 7: unconnected-(IC4-OSCIN-Pad7) -> /Motor_Controllers/CLK_SYNC
- IC4 pad 8: /Motor_Controllers/OSCOUT -> unconnected-(IC4-OSCOUT-Pad8)
- J17 pad 2: /Connectors/UART_TX -> unconnected-(J17-Pin_2-Pad2)
- J17 pad 3: /Connectors/UART_RX -> /Connectors/UART_TX
- Q1 pad 1: Net-(Q1-G) -> Net-(IC1-PGOOD)
- Q2 pad 1: +24V -> /Supply_24V/SW
- Q2 pad 2: +24V -> /Supply_24V/HO
- Q2 pad 3: /Supply_24V/HO -> +24V
- Q3 pad 1: /Supply_24V/SW -> GND
- Q3 pad 2: /Supply_24V/SW -> /Supply_24V/LO
- Q3 pad 3: /Supply_24V/LO -> /Supply_24V/SW
- Q4 pad 3: /Connectors/FAN_SW -> Net-(LED2-A1)
- Q5 pad 3: Net-(LED2-A1) -> Net-(LED2-A2)
- Q6 pad 3: Net-(LED2-A2) -> /Connectors/FAN_SW
- R1 pad 1: Net-(LED1-A) -> +5V
- R1 pad 2: +5V -> Net-(LED1-A)
- R10 pad 1: Net-(C12-Pad1) -> /Supply_24V/UVLO
- R10 pad 2: GND -> Net-(C12-Pad1)
- R11 pad 2: Net-(C12-Pad1) -> VCC
- R12 pad 1: /Supply_24V/UVLO -> /Supply_24V/COMP
- R12 pad 2: VCC -> Net-(C14-Pad1)
- R13 pad 1: /Supply_24V/COMP -> /Supply_24V/MODE
- R13 pad 2: Net-(C14-Pad1) -> /Supply_24V/VCC_REG
- R14 pad 2: /Supply_24V/VCC_DRIVER -> GND
- R15 pad 1: /Supply_24V/MODE -> +5V
- R15 pad 2: GND -> Net-(IC2-FB)
- R16 pad 1: VCC -> Net-(IC2-FB)
- R16 pad 2: Net-(IC2-EN) -> GND
- R17 pad 1: Net-(IC2-EN) -> VCC
- R17 pad 2: GND -> Net-(IC2-EN)
- R18 pad 1: +5V -> Net-(IC2-EN)
- R18 pad 2: Net-(IC2-FB) -> GND
- R19 pad 1: Net-(IC2-FB) -> /Motor_Controllers/ML_ADCIN
- R19 pad 2: GND -> +24V
- R20 pad 1: /Motor_Controllers/ML_ADCIN -> GND
- R20 pad 2: +24V -> /Motor_Controllers/ML_ADCIN
- R21 pad 1: Net-(C24-Pad2) -> /Motor_Controllers/MR_ADCIN
- R21 pad 2: /Motor_Controllers/ML_ADCIN -> +24V
- R22 pad 1: /Motor_Controllers/MR_ADCIN -> GND
- R22 pad 2: +24V -> /Motor_Controllers/MR_ADCIN
- R23 pad 1: Net-(C30-Pad2) -> +3.3V
- R23 pad 2: /Motor_Controllers/MR_ADCIN -> /Connectors/~{M_STBY}
- R24 pad 2: /Connectors/~{M_STBY} -> /Motor_Controllers/~{ML_BUSY}
- R25 pad 2: /Motor_Controllers/~{ML_BUSY} -> /Motor_Controllers/~{ML_FLAG}
- R26 pad 2: /Motor_Controllers/~{ML_FLAG} -> /Motor_Controllers/~{MR_BUSY}
- R27 pad 2: /Motor_Controllers/~{MR_BUSY} -> /Motor_Controllers/~{MR_FLAG}
- R28 pad 1: +3.3V -> GND
- R28 pad 2: /Motor_Controllers/~{MR_FLAG} -> /Connectors/LED_RED
- R29 pad 1: /Connectors/FAN_PWM -> /Connectors/LED_RED
- R29 pad 2: GND -> Net-(Q4-G)
- R3 pad 1: Net-(Q1-G) -> Net-(IC1-RT)
- R3 pad 2: Net-(IC1-PGOOD) -> GND
- R30 pad 1: /Connectors/FAN_PWM -> Net-(LED2-K1)
- R30 pad 2: Net-(Q4-G) -> +5V
- R31 pad 1: /Connectors/CELL_1 -> Net-(LED2-K2)
- R31 pad 2: Net-(IC6-AIN0) -> +5V
- R32 pad 1: Net-(IC6-AIN0) -> Net-(Q5-G)
- R32 pad 2: GND -> /Connectors/LED_GREEN
- R33 pad 1: /Connectors/CELL_2 -> /Connectors/LED_GREEN
- R33 pad 2: Net-(IC6-AIN1) -> GND
- R34 pad 1: Net-(IC6-AIN1) -> /Connectors/FAN_PWM
- R35 pad 1: /Connectors/CELL_3 -> /Connectors/FAN_PWM
- R35 pad 2: Net-(IC6-AIN2) -> Net-(Q6-G)
- R36 pad 1: Net-(IC6-AIN2) -> /Connectors/CELL_1
- R36 pad 2: GND -> Net-(IC6-AIN0)
- R37 pad 1: Net-(IC6-AIN3/REF) -> Net-(IC6-AIN0)
- R38 pad 1: GND -> /Connectors/CELL_2
- R38 pad 2: /Connectors/LED_RED -> Net-(IC6-AIN1)
- R39 pad 1: /Connectors/LED_RED -> Net-(IC6-AIN1)
- R39 pad 2: Net-(Q5-G) -> GND
- R4 pad 1: Net-(IC1-RT) -> VCC
- R4 pad 2: GND -> Net-(L1-Pad1)
- R40 pad 1: Net-(LED2-K1) -> /Connectors/CELL_3
- R40 pad 2: +5V -> Net-(IC6-AIN2)
- R41 pad 1: Net-(LED2-K2) -> Net-(IC6-AIN2)
- R41 pad 2: +5V -> GND
- R42 pad 1: Net-(Q6-G) -> Net-(IC6-AIN3/REF)
- R42 pad 2: /Connectors/LED_GREEN -> GND
- R5 pad 1: VCC -> /Supply_24V/CSN
- R6 pad 1: /Supply_24V/CSN -> /Supply_24V/VREF
- R6 pad 2: Net-(L1-Pad1) -> /Supply_24V/TRK
- R7 pad 1: /Supply_24V/VREF -> /Supply_24V/TRK
- R7 pad 2: /Supply_24V/TRK -> GND
- R8 pad 1: /Supply_24V/TRK -> VCC
- R8 pad 2: GND -> Net-(C12-Pad1)
- R9 pad 1: VCC -> Net-(C12-Pad1)
- R9 pad 2: Net-(C12-Pad1) -> GND
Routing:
- net +5V: track 0.00 -> 195.1 mm, vias 0 -> 4
- net +3.3V: track 0.00 -> 158.6 mm, vias 0 -> 8
- net /Connectors/I2C3_SDA: track 0.00 -> 124.8 mm
- net VCC: track 0.00 -> 106.4 mm, vias 0 -> 21
- net +24V: track 0.00 -> 106.3 mm, vias 0 -> 17
- net /Connectors/LED_GREEN: track 0.00 -> 87.3 mm, vias 0 -> 1
- net /Connectors/FAN_PWM: track 0.00 -> 87.2 mm, vias 0 -> 1
- net /Connectors/SPI_CLK: track 0.00 -> 83.4 mm, vias 0 -> 2
- net /Connectors/TOF1_EN: track 0.00 -> 78.5 mm
- net /Connectors/~{SPI_CS_E}: track 0.00 -> 78.4 mm
- net /Connectors/I2C3_SCL: track 0.00 -> 78.1 mm, vias 0 -> 1
- net /Connectors/UART_RX: track 0.00 -> 77.2 mm
- net /Connectors/LED_RED: track 0.00 -> 73.7 mm, vias 0 -> 1
- net GND: track 0.00 -> 72.6 mm, vias 4 -> 80
- net /Connectors/UART_TX: track 0.00 -> 71.8 mm
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- added copper zone on B.Cu, net +24V
- added copper zone on F.Cu, net +24V
- added copper zone on B.Cu, net +5V
- added copper zone on B.Cu, net /Connectors/CELL_1
- added copper zone on F.Cu, net /Connectors/CELL_2
- added copper zone on B.Cu, net /Connectors/CELL_3
- added copper zone on F.Cu, net /Supply_24V/SW
- added copper zone on In1.Cu, net GND
- added copper zone on In2.Cu, net GND
- added copper zone on B.Cu, net Net-(IC2-SW)
- added copper zone on F.Cu, net Net-(J6-Pin_1)
- added copper zone on F.Cu, net Net-(L1-Pad1)
- added copper zone on B.Cu, net VCC
- added copper zone on F.Cu, net VCC
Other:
- board size 65 x 56.5 mm -> 65 x 56 mm
- rule pad_to_mask_clearance: 0 -> 0.038
- board text added: "10A"
- board text added: "RyśBoard V6"
- board text removed: "Analog Ground Plane"
- board text removed: "Analog Power Plane"
- board text removed: "LLSMODE R3-FPWM R4-DEM"
- board text removed: "UNDERVOLTAGE LOCKOUT R12 - MONITOR MODE R13 - ALWAYS ENABLED R14 - MCU CONTROLLED"

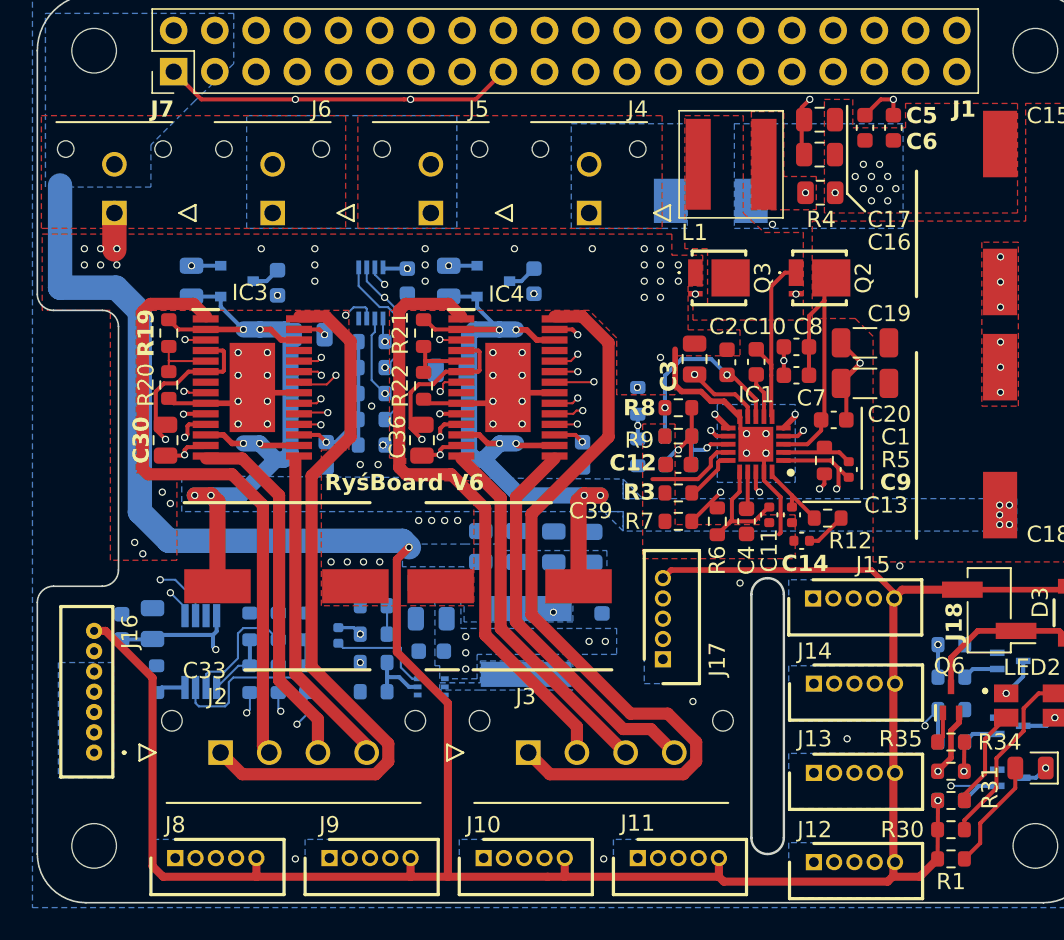
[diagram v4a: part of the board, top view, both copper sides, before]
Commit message: Trace routing corrections, prepared for further modifications
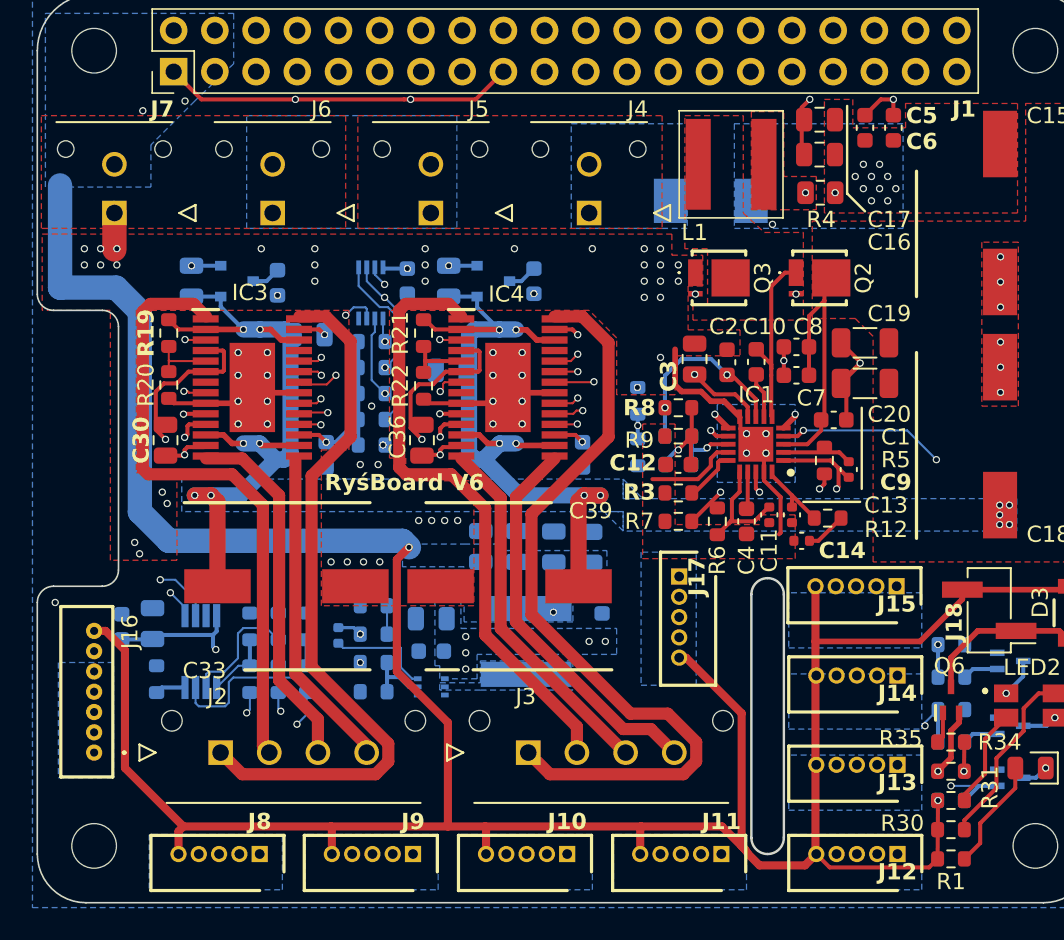
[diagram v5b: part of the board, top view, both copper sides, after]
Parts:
- J10, J11, J12, J13, J14, J15, J17, J8, J9: footprint parts:SHDR5W27P0X125_1X5_800X320X440P -> parts:530470510
- moved J8 5.21 mm to (35.2, 74.5), turned to 0 degrees
- moved J15 5.20 mm to (74.5, 58.0), turned to 0 degrees
- moved J17 5.20 mm to (61.0, 57.4), turned to 90 degrees
- moved J12 5.17 mm to (74.5, 74.5), turned to 0 degrees
- moved J13 5.17 mm to (74.5, 69.0), turned to 0 degrees
- moved J14 5.17 mm to (74.5, 63.5), turned to 0 degrees
- moved J10 5.16 mm to (54.1, 74.5), turned to 0 degrees
- moved J11 5.16 mm to (63.6, 74.5), turned to 0 degrees
- moved J9 5.16 mm to (44.6, 74.5), turned to 0 degrees
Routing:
- net /Connectors/I2C3_SCL: track 78.1 -> 123.9 mm, vias 1 -> 0
- net /Connectors/I2C3_SDA: track 124.8 -> 82.7 mm, vias 0 -> 1
- net /Connectors/TOF1_EN: track 78.5 -> 40.4 mm
- net /Connectors/TOF2_EN: track 67.2 -> 38.9 mm
- net /Connectors/I2C5_SCL: track 55.9 -> 36.0 mm
- net /Connectors/TOF3_EN: track 56.1 -> 36.6 mm
- net /Connectors/I2C5_SDA: track 58.3 -> 39.1 mm
- net /Connectors/TOF4_EN: track 54.2 -> 37.2 mm
- net Net-(IC1-PGOOD): track 47.8 -> 34.9 mm
- net /Connectors/TOF5_EN: track 43.4 -> 32.1 mm
- net /Connectors/UART_RX: track 77.2 -> 67.7 mm
- net /Connectors/TOF6_EN: track 35.3 -> 31.7 mm
- net /Connectors/~{SPI_CS_E}: track 78.4 -> 75.7 mm
- net /Connectors/I2C1_SDA: track 67.6 -> 65.2 mm
- net /Connectors/UART_TX: track 71.8 -> 70.3 mm
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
